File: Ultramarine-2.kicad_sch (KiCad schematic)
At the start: 124 parts, among them J1 OLED, J2 TRRS, J3 Flexible LED 3V, J4 Flexible LED GND, SW1 SW_Push, SW10 SW_Push, SW11 SW_Push, SW12 SW_Push, SW13 SW_Push, SW14 SW_Push, SW15 SW_Push, SW16 SW_Push, SW17 SW_Push, SW18 SW_Push, SW19 SW_Push, SW2 SW_Push, SW20 SW_Push, SW21 SW_Push, SW22 SW_Push, SW23 SW_Push, SW24 SW_Push, SW25 SW_Push, SW26 SW_Push, SW27 SW_Push, SW28 Extra, SW29 SW_Push, SW3 SW_Push, SW30 SW_Push, SW31 SW_Push, SW32 RotaryEncoder_Switch, SW33 Reset, SW34 Power Switch, SW4 SW_Push, SW5 SW_Push, SW6 SW_Push, SW7 SW_Push, SW8 SW_Push, SW9 SW_Push

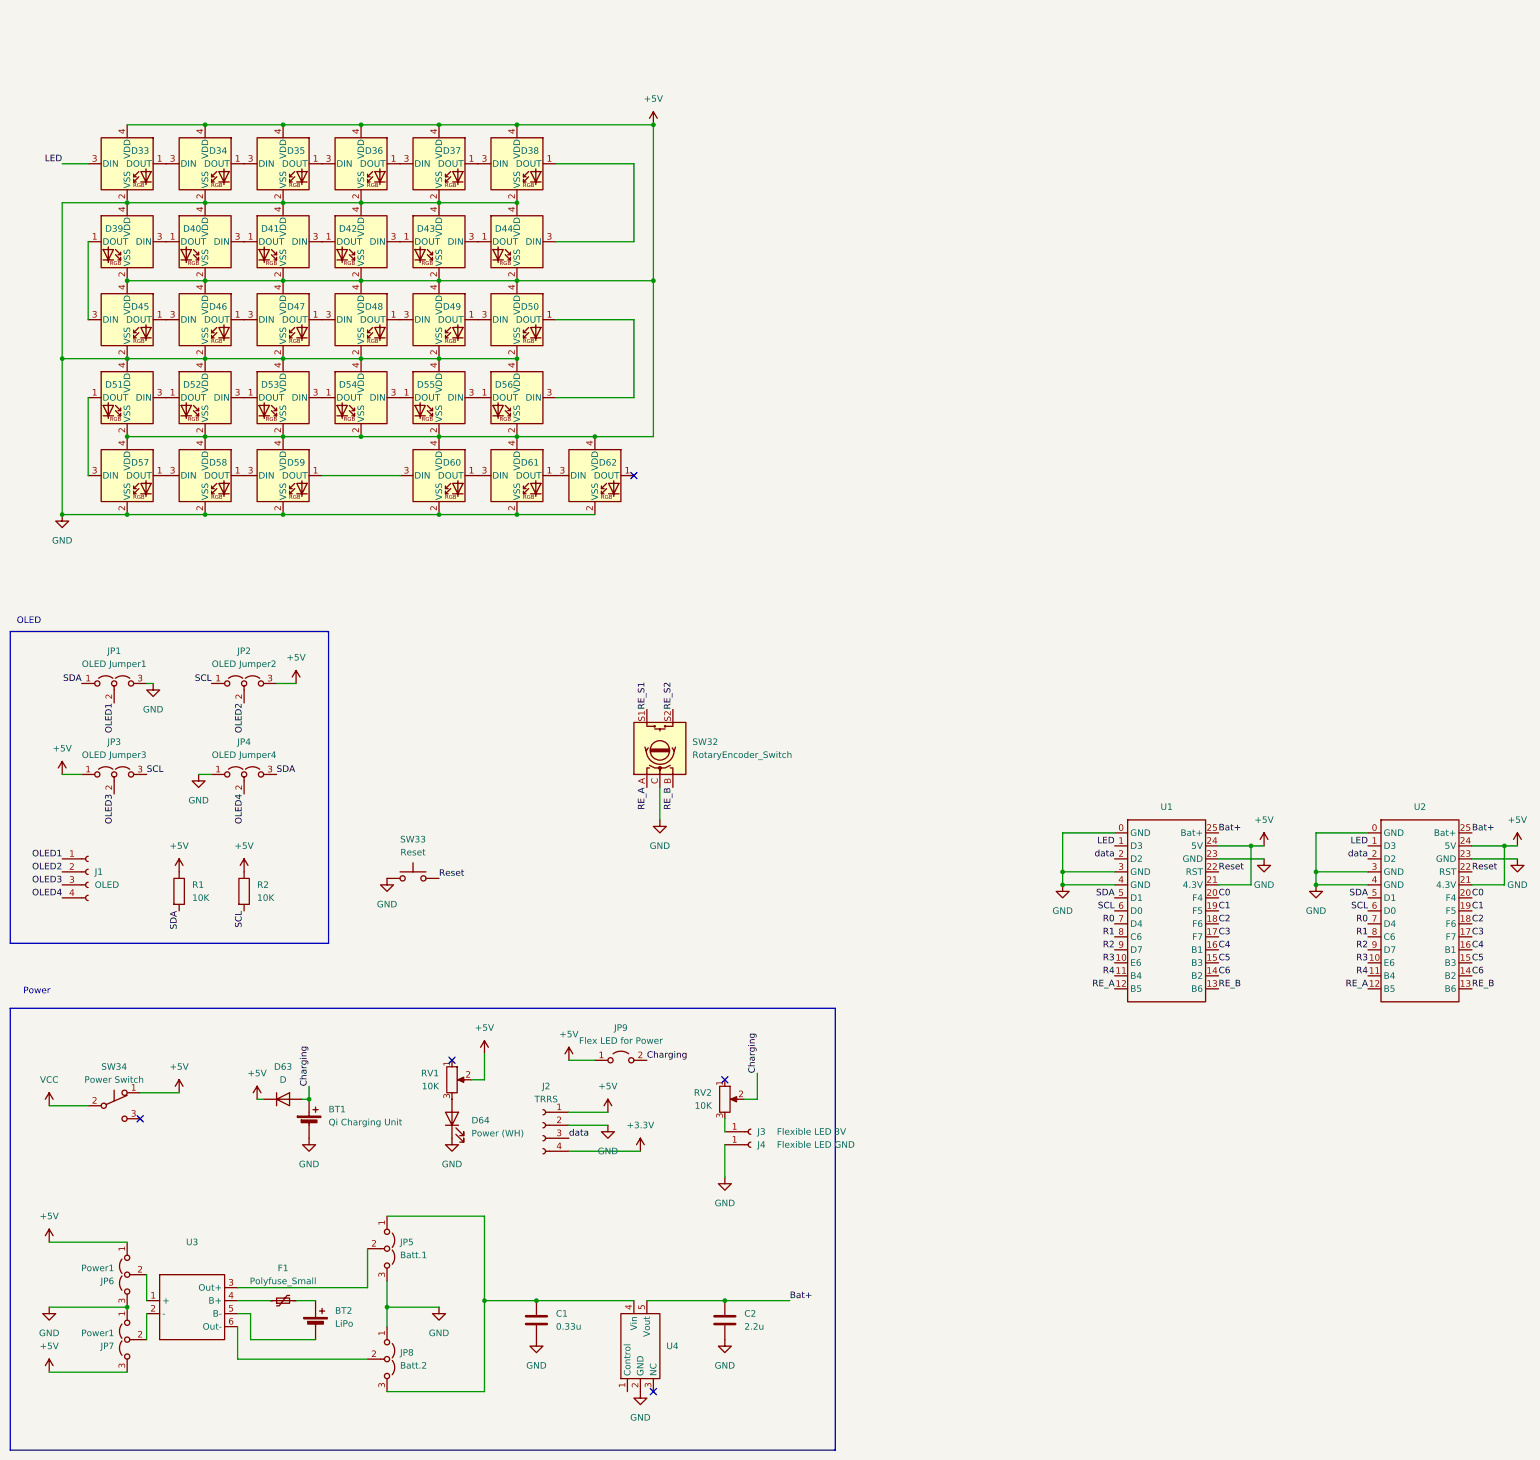
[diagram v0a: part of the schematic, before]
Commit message: make left hand type
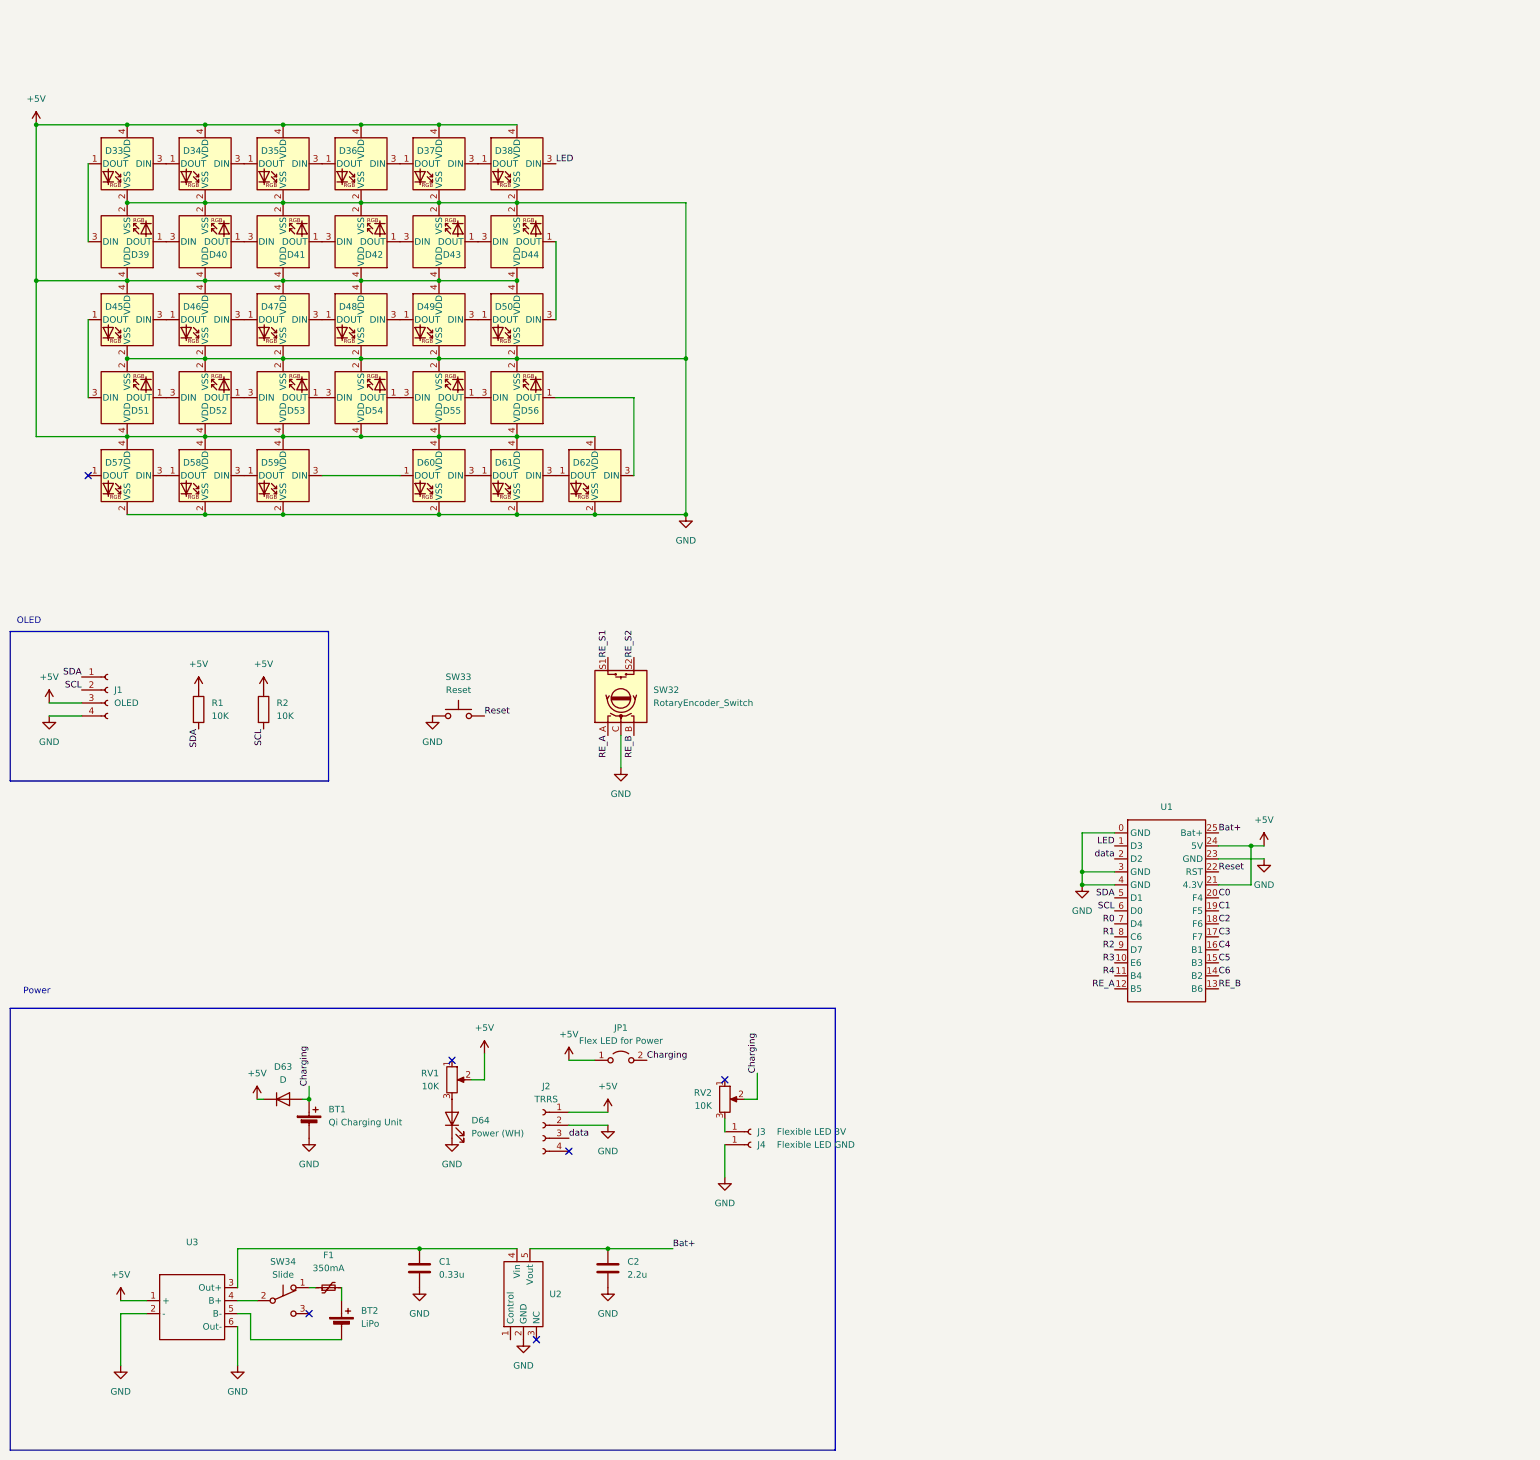
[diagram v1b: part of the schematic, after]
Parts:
- removed JP1: OLED Jumper1, Ultramarine-2:Jumper 3pin, symbol Jumper:Jumper_3_Open
- removed JP2: OLED Jumper2, Ultramarine-2:Jumper 3pin, symbol Jumper:Jumper_3_Open
- removed JP3: OLED Jumper3, Ultramarine-2:Jumper 3pin, symbol Jumper:Jumper_3_Open
- removed JP4: OLED Jumper4, Ultramarine-2:Jumper 3pin, symbol Jumper:Jumper_3_Open
- removed JP5: Batt.1, Ultramarine-2:Jumper 3pin, symbol Jumper:Jumper_3_Open
- removed JP6, JP7: Power1, Ultramarine-2:Jumper 3pin, symbol Jumper:Jumper_3_Open
- removed JP8: Batt.2, Ultramarine-2:Jumper 3pin, symbol Jumper:Jumper_3_Open
- removed U2: ~, Ultramarine-2:BLE Micro Pro, symbol Ultramarine-2:BLE_micro_Pro
- BT2: footprint (none) -> Ultramarine-2:Battery
- D1, D10, D11, D12, D13, D14, D15, D16, D17, D18, D19, D2, D20, D21, D22, D23, D24, D25, D26, D27, D28, D29, D3, D30, D31, D32, D4, D5, D6, D63, D7, D8, D9: footprint Ultramarine-2:SOD-123_reversible -> Ultramarine-2:SOD-123
- D33, D34, D35, D36, D37, D38, D39, D40, D41, D42, D43, D44, D45, D46, D47, D48, D49, D50, D51, D52, D53, D54, D55, D56, D57, D58, D59, D60, D61, D62: footprint Ultramarine-2:SK6812-mini_reversible -> Ultramarine-2:SK6812-mini
- D64: footprint Ultramarine-2:LED1608_reversible -> Ultramarine-2:LED1608
- F1: value Polyfuse_Small -> 350mA
- J1: footprint Connector_PinSocket_2.54mm:PinSocket_1x04_P2.54mm_Vertical -> Ultramarine-2:OLED
- J3, J4: footprint Connector_PinSocket_2.54mm:PinSocket_1x01_P2.54mm_Vertical -> Ultramarine-2:PTH_Flex_LED
- SW1, SW10, SW11, SW12, SW13, SW14, SW15, SW16, SW17, SW18, SW19, SW2, SW20, SW21, SW22, SW23, SW24, SW25, SW26, SW27, SW29, SW3, SW30, SW31, SW4, SW5, SW6, SW7, SW8, SW9: footprint Ultramarine-2:MX-Kailh -> Ultramarine-2:MX-hotswap
- SW32: footprint Rotary_Encoder:RotaryEncoder_Alps_EC12E-Switch_Vertical_H20mm -> Ultramarine-2:EC12
- SW34: value Power Switch -> Slide; footprint (none) -> Ultramarine-2:SK-12D11VG3
- renumbered JP9 to JP1, U4 to U2
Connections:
- net OLED1 is gone; now on net SDA: J1.1 (Pin_1)
- net OLED2 is gone; now on net SCL: J1.2 (Pin_2)
- net OLED3 is gone; now on net +5V: J1.3 (Pin_3)
- net OLED4 is gone; now on net GND: J1.4 (Pin_4)
- net +5V: now also D39.4 (VDD), D40.4 (VDD), D41.4 (VDD), D42.4 (VDD), D43.4 (VDD), D44.4 (VDD), D51.4 (VDD), D52.4 (VDD), D53.4 (VDD), D54.4 (VDD), D55.4 (VDD), D56.4 (VDD), U3.1 (+); no longer D39.2 (VSS), D40.2 (VSS), D41.2 (VSS), D42.2 (VSS), D43.2 (VSS), D44.2 (VSS), D51.2 (VSS), D52.2 (VSS), D53.2 (VSS), D54.2 (VSS), D55.2 (VSS), D56.2 (VSS), SW34.1 (A)
- net GND: now also D39.2 (VSS), D40.2 (VSS), D41.2 (VSS), D42.2 (VSS), D43.2 (VSS), D44.2 (VSS), D51.2 (VSS), D52.2 (VSS), D53.2 (VSS), D54.2 (VSS), D55.2 (VSS), D56.2 (VSS), U3.2 (-), U3.6 (Out-); no longer D39.4 (VDD), D40.4 (VDD), D41.4 (VDD), D42.4 (VDD), D43.4 (VDD), D44.4 (VDD), D51.4 (VDD), D52.4 (VDD), D53.4 (VDD), D54.4 (VDD), D55.4 (VDD), D56.4 (VDD)
- net LED: now also D38.3 (DIN); no longer D33.3 (DIN)
- net at D61.1 (DOUT): now also D60.3 (DIN); no longer D62.3 (DIN)
- net at D61.3 (DIN): now also D62.1 (DOUT); no longer D60.1 (DOUT)
- net at D37.1 (DOUT): now also D36.3 (DIN); no longer D38.3 (DIN)
- net at D37.3 (DIN): now also D38.1 (DOUT); no longer D36.1 (DOUT)
- net at D41.1 (DOUT): now also D42.3 (DIN); no longer D40.3 (DIN)
- net at D41.3 (DIN): now also D40.1 (DOUT); no longer D42.1 (DOUT)
- net at C1.1, U2.4 (Vin): now also U3.3 (Out+)
- net at D35.1 (DOUT): now also D34.3 (DIN); no longer D36.3 (DIN)
- net at F1.1: now also SW34.1 (A); no longer U3.4 (B+)
- net at D58.1 (DOUT): now also D57.3 (DIN); no longer D59.3 (DIN)
- net at D58.3 (DIN): now also D59.1 (DOUT); no longer D57.1 (DOUT)
- net at D55.1 (DOUT): now also D56.3 (DIN); no longer D54.3 (DIN)
- net at D55.3 (DIN): now also D54.1 (DOUT); no longer D56.1 (DOUT)
- net at D39.1 (DOUT): now also D40.3 (DIN); no longer D45.3 (DIN)
- net at D39.3 (DIN): now also D33.1 (DOUT); no longer D40.1 (DOUT)
- net at D35.3 (DIN): now also D36.1 (DOUT); no longer D34.1 (DOUT)
- net at D46.1 (DOUT): now also D45.3 (DIN); no longer D47.3 (DIN)
- net at D46.3 (DIN): now also D47.1 (DOUT); no longer D45.1 (DOUT)
- net at D53.1 (DOUT): now also D54.3 (DIN); no longer D52.3 (DIN)
- net at D53.3 (DIN): now also D52.1 (DOUT); no longer D54.1 (DOUT)
- net at D44.3 (DIN): now also D43.1 (DOUT); no longer D38.1 (DOUT)
- net at D49.1 (DOUT): now also D48.3 (DIN); no longer D50.3 (DIN)
- net at D49.3 (DIN): now also D50.1 (DOUT); no longer D48.1 (DOUT)
- net at D51.3 (DIN): now also D45.1 (DOUT); no longer D52.1 (DOUT)
- net at D43.3 (DIN): now also D42.1 (DOUT); no longer D44.1 (DOUT)
- net at D51.1 (DOUT): now also D52.3 (DIN); no longer D57.3 (DIN)
- net +3.3V: no longer names the net of J2.4 (Pin_4)
- net VCC: no longer names the net of SW34.2 (B)
- net VCC: now also U3.4 (B+)
- new net: D33.3 (DIN), D34.1 (DOUT)
- new net: D59.3 (DIN), D60.1 (DOUT)
- new net: D47.3 (DIN), D48.1 (DOUT)
- new net: D56.1 (DOUT), D62.3 (DIN)
- new net: D44.1 (DOUT), D50.3 (DIN)
- no-connect marks 5 -> 6
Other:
- moved on the sheet: BT2, C1, C2, F1, J1, R1, R2, SW32, SW33, SW34, U2

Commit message: starts build left hand
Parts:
- removed BT1: Qi Charging Unit, Ultramarine-2:Micro_USB_Charging, symbol Device:Battery_Cell
- removed BT2: LiPo, Ultramarine-2:Battery, symbol Device:Battery_Cell
- removed C1: 0.33u, Capacitor_SMD:C_0603_1608Metric, symbol Device:C
- removed C2: 2.2u, Capacitor_SMD:C_0603_1608Metric, symbol Device:C
- removed D29, D63: D, Ultramarine-2:SOD-123, symbol Device:D
- removed D64: Power (WH), Ultramarine-2:LED1608, symbol Device:LED
- removed F1: 350mA, Ultramarine-2:MF-NSMF, symbol Device:Polyfuse_Small
- removed J2: TRRS, Ultramarine-2:MJ-4PP-9, symbol Connector:Conn_01x04_Socket
- removed J3: Flexible LED 3V, Ultramarine-2:PTH_Flex_LED, symbol Connector:Conn_01x01_Socket
- removed J4: Flexible LED GND, Ultramarine-2:PTH_Flex_LED, symbol Connector:Conn_01x01_Socket
- removed RV1, RV2: 10K, Ultramarine-2:R_variable, symbol Device:R_Potentiometer
- removed SW28: Extra, Ultramarine-2:Tactlie_Switch, symbol Switch:SW_Push
- removed SW34: Slide, Ultramarine-2:SK-12D11VG3, symbol Switch:SW_Push_SPDT
- removed U2: ~, Package_TO_SOT_SMD:SOT-89-5, symbol Ultramarine-2:NJM2884
- removed U3: ~, Ultramarine-2:TP4056, symbol Ultramarine-2:TP4056
- added J2: Generic_connector, Connector_PinHeader_2.54mm:PinHeader_1x05_P2.54mm_Horizontal, symbol Connector:Conn_01x05_Socket
- added J3: Flex LED 3V, Ultramarine-2:PTH_Flex_LED, symbol Connector:Conn_01x01_Pin
- added J4: Flex LED GND, Ultramarine-2:PTH_Flex_LED, symbol Connector:Conn_01x01_Pin
- renumbered D30 to D29, D31 to D30, D32 to D31, D33 to D32, D34 to D33, D35 to D34, D36 to D35, D37 to D36, D38 to D37, D39 to D38, D40 to D39, D41 to D40, D42 to D41, D43 to D42, D44 to D43, D45 to D44, D46 to D45, D47 to D46, D48 to D47, D49 to D48, D50 to D49, D51 to D50, D52 to D51, D53 to D52, D54 to D53, D55 to D54, D56 to D55, D57 to D56, D58 to D57, D59 to D58, D60 to D59, D61 to D60, D62 to D61, SW29 to SW28, SW30 to SW29, SW31 to SW30, SW32 to SW31, SW33 to SW32
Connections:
- net +5V: now also J2.1 (Pin_1); no longer U1.21 (4.3V)
- net Bat+: now also J2.2 (Pin_2)
- net C0: now also SW1.2, SW13.2, SW19.2, SW25.2, SW7.2; no longer SW1.1, SW13.1, SW19.1, SW25.1, SW7.1
- net C1: now also SW14.2, SW2.2, SW20.2, SW26.2, SW8.2; no longer SW14.1, SW2.1, SW20.1, SW26.1, SW8.1
- net C2: now also SW15.2, SW21.2, SW27.2, SW3.2, SW9.2; no longer SW15.1, SW21.1, SW27.1, SW3.1, SW9.1
- net C3: now also SW10.2, SW16.2, SW22.2, SW4.2; no longer SW10.1, SW16.1, SW22.1, SW4.1
- net C4: now also SW11.2, SW17.2, SW23.2, SW5.2; no longer SW11.1, SW17.1, SW23.1, SW5.1
- net C5: now also SW12.2, SW18.2, SW24.2, SW6.2; no longer SW12.1, SW18.1, SW24.1, SW6.1
- net GND: now also J2.5 (Pin_5), J4.1 (Pin_1)
- net data: now also J2.4 (Pin_4)
- net at D5.2 (A): now also SW5.1; no longer SW5.2
- net at D17.2 (A): now also SW17.1; no longer SW17.2
- net at D12.2 (A): now also SW12.1; no longer SW12.2
- net at D11.2 (A): now also SW11.1; no longer SW11.2
- net at D19.2 (A): now also SW19.1; no longer SW19.2
- net at D24.2 (A): now also SW24.1; no longer SW24.2
- net at D26.2 (A): now also SW25.1; no longer SW25.2
- net at D28.2 (A): now also SW27.1; no longer SW27.2
- net at D15.2 (A): now also SW15.1; no longer SW15.2
- net at D23.2 (A): now also SW23.1; no longer SW23.2
- net at D7.2 (A): now also SW7.1; no longer SW7.2
- net at D27.2 (A): now also SW26.1; no longer SW26.2
- net at D13.2 (A): now also SW13.1; no longer SW13.2
- net at D16.2 (A): now also SW16.1; no longer SW16.2
- net at D21.2 (A): now also SW21.1; no longer SW21.2
- net at D22.2 (A): now also SW22.1; no longer SW22.2
- net at D1.2 (A): now also SW1.1; no longer SW1.2
- net at D10.2 (A): now also SW10.1; no longer SW10.2
- net at D4.2 (A): now also SW4.1; no longer SW4.2
- net at D2.2 (A): now also SW2.1; no longer SW2.2
- net at D14.2 (A): now also SW14.1; no longer SW14.2
- net at D3.2 (A): now also SW3.1; no longer SW3.2
- net at D6.2 (A): now also SW6.1; no longer SW6.2
- net at D9.2 (A): now also SW9.1; no longer SW9.2
- net at D8.2 (A): now also SW8.1; no longer SW8.2
- net at D18.2 (A): now also SW18.1; no longer SW18.2
- net at D20.2 (A): now also SW20.1; no longer SW20.2
- new net: J2.3 (Pin_3), J3.1 (Pin_1)
- no-connect marks 6 -> 1
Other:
- note removed: "Power"
- moved on the sheet: D1, D10, D11, D12, D13, D14, D15, D16, D17, D18, D19, D2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

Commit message: reversible type
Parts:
- added JP1, JP2, JP3, JP4, JP5, JP6: Jumper_3_Open, Ultramarine-2:Jumper 3pin, symbol Jumper:Jumper_3_Open
- added U2: ~, Ultramarine-2:BLE Micro Pro, symbol Ultramarine-2:BLE_micro_Pro
- J3: renamed from J2; footprint Connector_PinHeader_2.54mm:PinHeader_1x05_P2.54mm_Horizontal -> Ultramarine-2:5pin
- SW1, SW10, SW11, SW12, SW13, SW14, SW15, SW16, SW17, SW18, SW19, SW2, SW20, SW21, SW22, SW23, SW24, SW25, SW26, SW27, SW28, SW29, SW3, SW30, SW4, SW5, SW6, SW7, SW8, SW9: footprint Ultramarine-2:MX-hotswap -> Ultramarine-2:MX-hotswap_reversible
- renumbered J3 to J2, JP1 to JP7
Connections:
- net +5V: now also JP2.3 (B), JP5.1 (A), U2.24 (5V); no longer J1.3 (Pin_3)
- net Bat+: now also U2.25 (Bat+)
- net C0: now also U1.19 (F5), U2.19 (F5); no longer U1.20 (F4)
- net C1: now also U1.7 (D4), U2.7 (D4); no longer U1.19 (F5)
- net C2: now also U1.16 (B1), U2.16 (B1); no longer U1.18 (F6)
- net C3: now also U1.10 (E6), U2.10 (E6); no longer U1.17 (F7)
- net C4: now also U1.18 (F6), U2.18 (F6); no longer U1.16 (B1)
- net C5: now also U1.8 (C6), U2.8 (C6); no longer U1.15 (B3)
- net C6: now also U2.14 (B2)
- net GND: now also JP1.3 (B), JP6.1 (A), U2.0 (GND), U2.23 (GND), U2.3 (GND), U2.4 (GND); no longer J1.4 (Pin_4)
- net LED: now also U2.1 (D3)
- net R0: now also U1.20 (F4), U2.20 (F4); no longer U1.7 (D4)
- net R1: now also U1.17 (F7), U2.17 (F7); no longer U1.8 (C6)
- net R2: now also U2.9 (D7)
- net R3: now also U1.15 (B3), U2.15 (B3); no longer U1.10 (E6)
- net R4: now also U2.11 (B4)
- net RE_A: now also JP3.1 (A), JP4.3 (B), U2.12 (B5); no longer SW31.A
- net RE_B: now also JP3.3 (B), JP4.1 (A), U2.13 (B6); no longer SW31.B
- net Reset: now also U2.22 (RST)
- net SCL: now also JP2.1 (A), JP5.3 (B), U2.6 (D0); no longer J1.2 (Pin_2)
- net SDA: now also JP1.1 (A), JP6.3 (B), U2.5 (D1); no longer J1.1 (Pin_1)
- net data: now also U2.2 (D2)
- new net: J1.1 (Pin_1), JP1.2 (C)
- new net: J1.2 (Pin_2), JP2.2 (C)
- new net: J1.3 (Pin_3), JP5.2 (C)
- new net: J1.4 (Pin_4), JP6.2 (C)
- new net: JP3.2 (C), SW31.A
- new net: JP4.2 (C), SW31.B
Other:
- moved on the sheet: J1, J2, J3, J4, JP7, R1, R2
